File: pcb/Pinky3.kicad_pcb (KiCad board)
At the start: 2 copper layers, 137 x 100.9 mm, 65 parts, among them J1 MJ-4PP-9, P1 i2c-pin, P2 i2c-pin, SW1 RESET_SW, SW10 SW_PUSH, SW11 SW_PUSH, SW12 SW_PUSH, SW13 SW_PUSH, SW14 SW_PUSH, SW15 SW_PUSH, SW16 SW_PUSH, SW17 SW_PUSH, SW18 SW_PUSH, SW19 SW_PUSH, SW2 SW_PUSH, SW20 SW_PUSH, SW21 SW_PUSH, SW22 SW_PUSH, SW23 SW_PUSH, SW24 SW_PUSH, SW25 SW_PUSH, SW26 SW_PUSH, SW3 SW_PUSH, SW4 SW_PUSH, SW5 SW_PUSH, SW6 SW_PUSH, SW7 SW_PUSH, SW8 SW_PUSH, SW9 SW_PUSH, U1 ProMicro

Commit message: tweak
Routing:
- net Net-(J1-PadB): track 125.4 -> 126.1 mm
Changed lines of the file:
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@@
     (thickness 1.6)
     (drawings 163)
-    (tracks 955)
+    (tracks 953)
     (zones 0)
     (modules 65)
@@
     (38 B.Mask user)
     (39 F.Mask user)
-    (40 Dwgs.User user hide)
+    (40 Dwgs.User user)
     (41 Cmts.User user)
     (42 Eco1.User user)
@@
   (segment (start 164.9 107.95) (end 164.9 105.5) (width 0.25) (layer F.Cu) (net 28))
   (segment (start 102.831509 116.226489) (end 98.2 120.857998) (width 0.25) (layer F.Cu) (net 29))
-  (segment (start 98.2 133.521002) (end 96.196001 135.525001) (width 0.25) (layer F.Cu) (net 29))
-  (segment (start 98.2 120.857998) (end 98.2 133.521002) (width 0.25) (layer F.Cu) (net 29))
-  (segment (start 81.8215 134.30038) (end 81 134.30038) (width 0.25) (layer F.Cu) (net 29) (status 20))
-  (segment (start 83.046121 135.525001) (end 81.8215 134.30038) (width 0.25) (layer F.Cu) (net 29))
-  (segment (start 87.9 135.525001) (end 87.774999 135.525001) (width 0.25) (layer F.Cu) (net 29))
-  (segment (start 96.196001 135.525001) (end 87.9 135.525001) (width 0.25) (layer F.Cu) (net 29))
-  (segment (start 86.574999 135.525001) (end 86.5 135.525001) (width 0.25) (layer F.Cu) (net 29))
-  (segment (start 92.4 129.7) (end 86.574999 135.525001) (width 0.25) (layer F.Cu) (net 29) (status 10))
-  (segment (start 86.5 135.525001) (end 83.046121 135.525001) (width 0.25) (layer F.Cu) (net 29))
-  (segment (start 87.9 135.525001) (end 86.5 135.525001) (width 0.25) (layer F.Cu) (net 29))
   (segment (start 166.503122 116.196878) (end 173 109.7) (width 0.25) (layer F.Cu) (net 29))
   (segment (start 173 109.7) (end 173.4 109.7) (width 0.25) (layer F.Cu) (net 29))
@@
   (segment (start 102.831509 116.226489) (end 162.773511 116.226489) (width 0.25) (layer F.Cu) (net 29))
   (segment (start 173.4 109.7) (end 173.4 103.75) (width 0.25) (layer F.Cu) (net 29))
+  (segment (start 81.015121 134.315501) (end 81 134.315501) (width 0.25) (layer F.Cu) (net 29))
+  (segment (start 98.2 134.071002) (end 96.496001 135.775001) (width 0.25) (layer F.Cu) (net 29))
+  (segment (start 82.474621 135.775001) (end 81.015121 134.315501) (width 0.25) (layer F.Cu) (net 29))
+  (segment (start 98.2 120.857998) (end 98.2 134.071002) (width 0.25) (layer F.Cu) (net 29))
+  (segment (start 92.4 129.7) (end 86.324999 135.775001) (width 0.25) (layer F.Cu) (net 29))
+  (segment (start 86.324999 135.775001) (end 86.3 135.775001) (width 0.25) (layer F.Cu) (net 29))
+  (segment (start 86.3 135.775001) (end 82.474621 135.775001) (width 0.25) (layer F.Cu) (net 29))
+  (segment (start 96.496001 135.775001) (end 86.3 135.775001) (width 0.25) (layer F.Cu) (net 29))
   (via (at 157.9 81.9) (size 0.6) (drill 0.4) (layers F.Cu B.Cu) (net 30))
   (segment (start 52.432 118.1436) (end 49.892 118.1436) (width 0.5) (layer B.Cu) (net 30) (status 30))

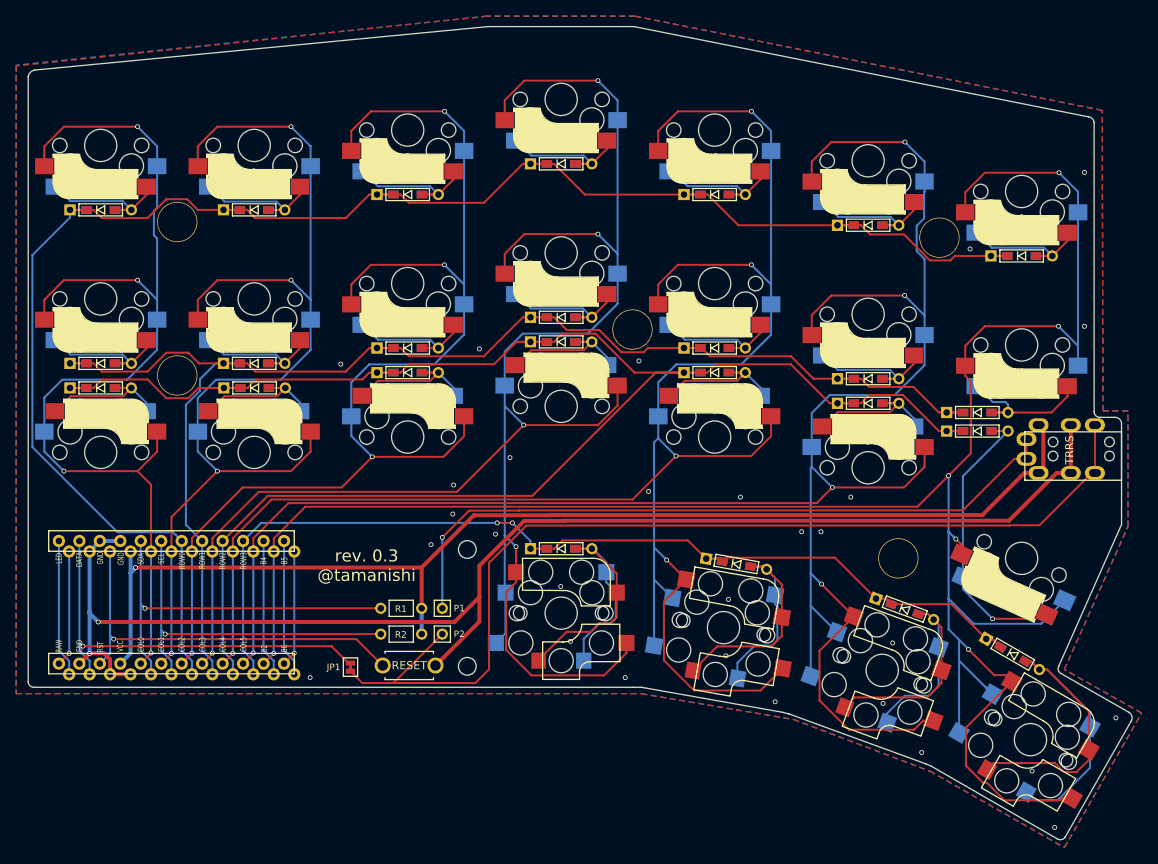
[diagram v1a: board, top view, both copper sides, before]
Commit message: - add images - add logo - change thumb keys footprints to choc only
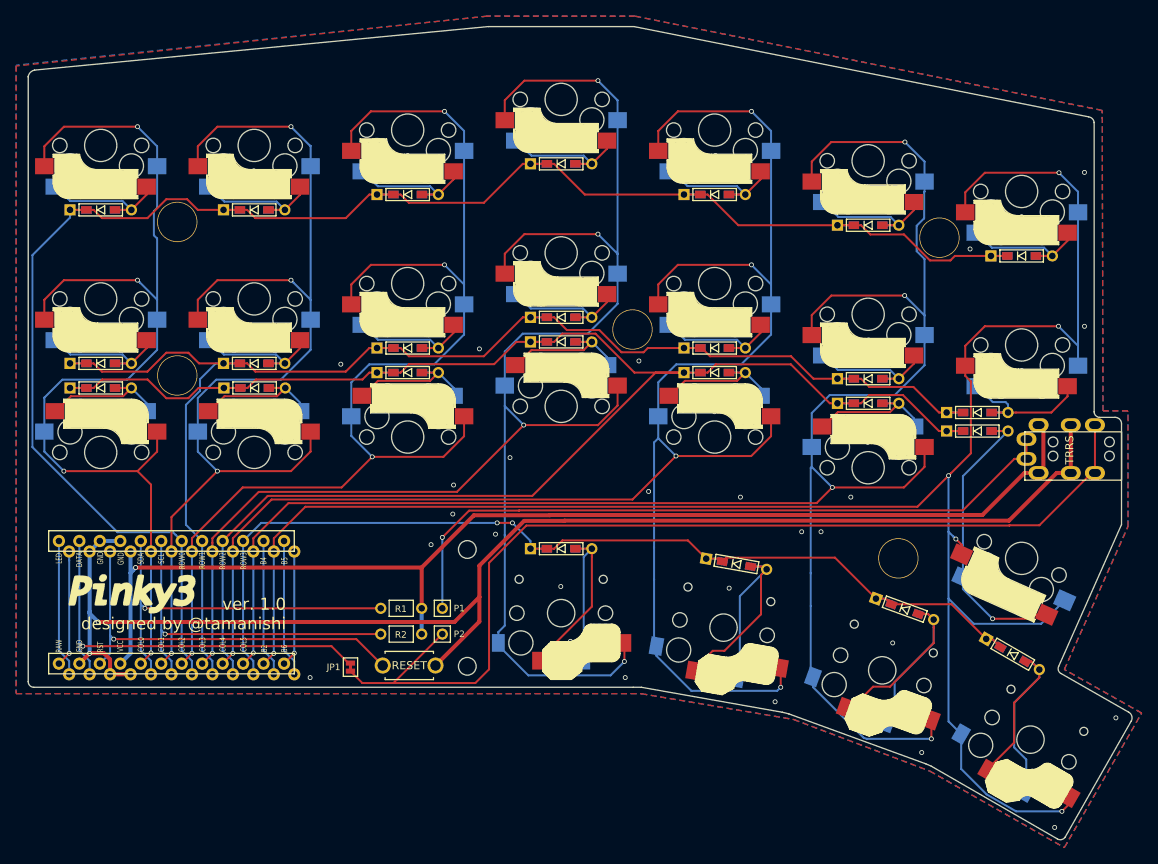
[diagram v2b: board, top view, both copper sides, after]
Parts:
- added G***: LOGO, lib:pinky3, B.Cu at (64.6, 125.7)
- added G***: LOGO, lib:pinky3, F.Cu at (53.9, 124.7)
- SW14, SW18, SW22, SW26: footprint kbd:CherryMX_KailhLowProfile_Hotswap -> kbd:Choc_Hotswap
- turned SW14 to 180 degrees
- turned SW18 to 170 degrees
- turned SW22 to 160 degrees
- turned SW26 to 150 degrees
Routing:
- net Net-(D25-Pad2): track 58.1 -> 36.6 mm
- net col6: track 272.0 -> 250.7 mm
- net col5: track 261.9 -> 242.4 mm
- net col4: track 243.4 -> 226.4 mm
- net col3: track 228.4 -> 214.8 mm
- net Net-(D13-Pad2): track 43.7 -> 35.3 mm
- net Net-(D17-Pad2): track 43.6 -> 36.5 mm, vias 1 -> 0
- net Net-(D21-Pad2): track 43.4 -> 36.8 mm
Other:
- board text added: "ver. 1.0 designed by @tamanishi"
- board text removed: "rev. 0.3 @tamanishi"

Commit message: create branch
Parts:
- D1, D10, D11, D12, D13, D14, D15, D16, D17, D18, D19, D2, D20, D21, D22, D23, D24, D25, D3, D4, D5, D6, D7, D8, D9: footprint kbd:D3_TH_SMD -> kbd:D3_SMD
- SW10, SW11, SW12, SW13, SW15, SW16, SW17, SW19, SW2, SW20, SW21, SW23, SW24, SW25, SW3, SW4, SW5, SW6, SW7, SW8, SW9: footprint kbd:CherryMX_Hotswap -> kbd:Choc_Hotswap
- moved D5 18.0 mm to (73.0, 78.5)
- moved D2 17.6 mm to (50.0, 78.5), turned to 180 degrees
- moved D4 4.25 mm to (65.0, 78.5)
- moved D3 1.55 mm to (50.0, 97.6)
- moved D1 0.55 mm to (50.0, 76.5), turned to 180 degrees
- turned SW11 to 0 degrees
- turned SW12 to 0 degrees
- turned SW15 to 0 degrees
- turned SW16 to 0 degrees
- turned SW19 to 0 degrees
- turned SW2 to 0 degrees
- turned SW20 to 0 degrees
- turned SW23 to 0 degrees
- turned SW24 to 0 degrees
- turned SW3 to 0 degrees
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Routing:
- net row0: track 213.6 -> 161.3 mm, vias 0 -> 1
- net row2: track 219.4 -> 204.1 mm
- net row1: track 178.9 -> 166.2 mm, vias 0 -> 1
- net Net-(D3-Pad2): track 18.6 -> 10.4 mm
- net Net-(D2-Pad2): track 18.4 -> 11.6 mm, vias 0 -> 2
- net Net-(D1-Pad2): track 18.7 -> 23.4 mm, vias 0 -> 2
- net col0: track 129.3 -> 133.4 mm, vias 4 -> 2

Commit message: [WIP] worked for Choc and XSwitch PCB design
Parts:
- SW14, SW18, SW22, SW26: footprint kbd:Choc_Hotswap -> lib:Kailh-PG1425-X-Switch-reversible
- moved D23 18.4 mm to (164.3, 84.6)
- moved D15 17.3 mm to (126.2, 76.9)
- moved D8 17.3 mm to (88.1, 76.9)
- moved D11 17.3 mm to (107.2, 73.1)
- moved D19 17.2 mm to (145.2, 80.8)
- moved D4 4.32 mm to (69.1, 77.0)
- moved D5 3.96 mm to (69.1, 78.8)
- moved D20 1.56 mm to (145.2, 99.5)
- moved D6 1.55 mm to (69.1, 97.6)
- moved D16 1.55 mm to (126.2, 95.7)
- moved D9 1.55 mm to (88.1, 95.7)
- moved D12 1.53 mm to (107.2, 91.9)
- moved D24 1.22 mm to (159.0, 103.3)
- moved D1 0.50 mm to (50.0, 77.0), turned to 0 degrees
- moved D2 0.30 mm to (50.0, 78.8), turned to 0 degrees
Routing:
- net row0: track 161.3 -> 196.1 mm, vias 1 -> 7
- net Net-(D21-Pad2): track 36.8 -> 15.1 mm, vias 0 -> 1
- net row1: track 166.2 -> 187.8 mm, vias 1 -> 7
- net Net-(D17-Pad2): track 36.5 -> 15.4 mm, vias 0 -> 1
- net Net-(D13-Pad2): track 35.3 -> 15.0 mm, vias 0 -> 1
- net Net-(D25-Pad2): track 36.6 -> 19.2 mm, vias 0 -> 1
- net col3: track 214.8 -> 198.5 mm
- net col5: track 242.4 -> 228.1 mm, vias 5 -> 4
- net col4: track 226.4 -> 217.1 mm, vias 5 -> 4
- net row3: track 128.8 -> 120.0 mm, vias 2 -> 6
- net Net-(D23-Pad2): track 19.6 -> 11.1 mm, vias 0 -> 2
- net Net-(D24-Pad2): track 38.2 -> 29.8 mm, vias 1 -> 2
- net Net-(D15-Pad2): track 18.4 -> 10.3 mm, vias 0 -> 2
- net Net-(D11-Pad2): track 18.4 -> 10.5 mm, vias 0 -> 2
- net Net-(D9-Pad2): track 18.6 -> 11.0 mm, vias 0 -> 2
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
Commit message: prototype pcb ordered
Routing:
- net col6: track 248.4 -> 253.8 mm
- net col5: track 228.1 -> 232.2 mm
- net row2: track 203.6 -> 200.4 mm
- net col3: track 198.5 -> 201.4 mm, vias 5 -> 4
- net col4: track 217.1 -> 214.4 mm
- net Net-(J1-PadB): track 126.1 -> 127.2 mm
- net GND: track 175.2 -> 176.0 mm
- net row3: track 120.0 -> 119.2 mm
- net VCC: track 147.1 -> 147.8 mm
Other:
- board text added: "ver. 1.0a designed by @tamanishi"
- board text removed: "ver. 1.0 designed by @tamanishi"

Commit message: tweak row2
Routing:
- net row2: track 200.4 -> 192.3 mm
- net col3: track 201.4 -> 204.8 mm, vias 4 -> 5
- net col2: track 145.2 -> 144.2 mm
- net GND: vias 56 -> 57
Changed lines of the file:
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@@
     (thickness 1.6)
     (drawings 29)
-    (tracks 910)
+    (tracks 912)
     (zones 0)
     (modules 67)
@@
   (segment (start 154.85 103.3) (end 156.325 103.3) (width 0.25) (layer F.Cu) (net 7))
   (segment (start 152.32499 100.77499) (end 154.85 103.3) (width 0.25) (layer F.Cu) (net 7))
-  (segment (start 113.876999 102.023001) (end 120.175 95.725) (width 0.25) (layer F.Cu) (net 7))
-  (segment (start 113.875001 102.023001) (end 113.876999 102.023001) (width 0.25) (layer F.Cu) (net 7))
-  (segment (start 103.073012 112.82499) (end 113.875001 102.023001) (width 0.25) (layer F.Cu) (net 7))
-  (segment (start 70.45061 112.82499) (end 103.073012 112.82499) (width 0.25) (layer F.Cu) (net 7))
-  (segment (start 65.132 118.1436) (end 70.45061 112.82499) (width 0.25) (layer F.Cu) (net 7))
   (segment (start 120.175 95.725) (end 115.643998 95.725) (width 0.25) (layer F.Cu) (net 7))
   (segment (start 120.175 95.725) (end 124.375 95.725) (width 0.25) (layer F.Cu) (net 7))
+  (segment (start 66.90061 116.37499) (end 65.893999 117.381601) (width 0.25) (layer B.Cu) (net 7))
+  (segment (start 65.893999 117.381601) (end 65.132 118.1436) (width 0.25) (layer B.Cu) (net 7))
+  (segment (start 89.550012 116.37499) (end 66.90061 116.37499) (width 0.25) (layer B.Cu) (net 7))
+  (segment (start 97.025001 108.900001) (end 89.550012 116.37499) (width 0.25) (layer B.Cu) (net 7))
+  (segment (start 97.025001 100.274999) (end 97.025001 108.900001) (width 0.25) (layer B.Cu) (net 7))
+  (segment (start 105.375 91.925) (end 97.025001 100.274999) (width 0.25) (layer B.Cu) (net 7))
   (segment (start 89.7 74.8) (end 89.875 74.8) (width 0.25) (layer B.Cu) (net 8))
   (segment (start 85.3 70.4) (end 89.7 74.8) (width 0.25) (layer B.Cu) (net 8))
@@
   (via (at 144.575 113.525) (size 0.6) (drill 0.4) (layers F.Cu B.Cu) (net 30))
   (via (at 70.475 115.125) (size 0.6) (drill 0.4) (layers F.Cu B.Cu) (net 30))
-  (via (at 65.875 114.625) (size 0.6) (drill 0.4) (layers F.Cu B.Cu) (net 30))
   (via (at 163.175 111.625) (size 0.6) (drill 0.4) (layers F.Cu B.Cu) (net 30))
+  (via (at 65.575 114.625) (size 0.6) (drill 0.4) (layers F.Cu B.Cu) (net 30))
+  (via (at 68.175 114.625) (size 0.6) (drill 0.4) (layers F.Cu B.Cu) (net 30))
   (segment (start 48.622 133.024838) (end 48.622 134.69) (width 0.25) (layer B.Cu) (net 31) (status 20))
   (segment (start 47.352 131.754838) (end 48.622 133.024838) (width 0.25) (layer B.Cu) (net 31))
@@
   (segment (start 95.85 89.2) (end 95.9 89.2) (width 0.25) (layer B.Cu) (net 38))
   (segment (start 95.9 70.4) (end 95.9 89.2) (width 0.25) (layer B.Cu) (net 38))
-  (segment (start 80.2 101.545) (end 80.2 104.198998) (width 0.25) (layer F.Cu) (net 38))
-  (segment (start 95.9 104.758002) (end 93.333002 107.325) (width 0.25) (layer B.Cu) (net 38))
-  (segment (start 95.9 101.545) (end 95.9 104.758002) (width 0.25) (layer B.Cu) (net 38))
-  (via (at 77.074499 107.324499) (size 0.6) (drill 0.4) (layers F.Cu B.Cu) (net 38))
-  (segment (start 77.075 107.325) (end 77.074499 107.324499) (width 0.25) (layer B.Cu) (net 38))
-  (segment (start 93.333002 107.325) (end 77.075 107.325) (width 0.25) (layer B.Cu) (net 38))
-  (segment (start 80.2 104.198998) (end 77.074499 107.324499) (width 0.25) (layer F.Cu) (net 38))
   (segment (start 61.322 119.45) (end 61.322 132.078) (width 0.25) (layer B.Cu) (net 38))
   (via (at 61.322 132.078) (size 0.6) (drill 0.4) (layers F.Cu B.Cu) (net 38))
   (segment (start 61.322 132.0936) (end 60.052 133.3636) (width 0.25) (layer F.Cu) (net 38))
   (segment (start 61.322 132.078) (end 61.322 132.0936) (width 0.25) (layer F.Cu) (net 38))
-  (segment (start 61.322 117.804838) (end 61.322 118.37237) (width 0.25) (layer F.Cu) (net 38))
   (segment (start 61.322 118.37237) (end 61.322 119.45) (width 0.25) (layer F.Cu) (net 38))
-  (segment (start 67.376858 111.74998) (end 61.322 117.804838) (width 0.25) (layer F.Cu) (net 38))
-  (segment (start 72.649018 111.74998) (end 67.376858 111.74998) (width 0.25) (layer F.Cu) (net 38))
-  (segment (start 77.074499 107.324499) (end 72.649018 111.74998) (width 0.25) (layer F.Cu) (net 38))
+  (segment (start 66.926848 112.19999) (end 61.322 117.804838) (width 0.25) (layer F.Cu) (net 38))
+  (segment (start 61.322 117.804838) (end 61.322 118.37237) (width 0.25) (layer F.Cu) (net 38))
+  (segment (start 74.641012 112.19999) (end 66.926848 112.19999) (width 0.25) (layer F.Cu) (net 38))
+  (segment (start 80.2 101.545) (end 80.2 106.641002) (width 0.25) (layer F.Cu) (net 38))
+  (segment (start 95.9 104.758002) (end 93.333002 107.325) (width 0.25) (layer B.Cu) (net 38))
+  (segment (start 95.9 101.545) (end 95.9 104.758002) (width 0.25) (layer B.Cu) (net 38))
+  (segment (start 79.516002 107.325) (end 79.495501 107.345501) (width 0.25) (layer B.Cu) (net 38))
+  (segment (start 93.333002 107.325) (end 79.516002 107.325) (width 0.25) (layer B.Cu) (net 38))
+  (segment (start 79.495501 107.345501) (end 74.641012 112.19999) (width 0.25) (layer F.Cu) (net 38))
+  (via (at 79.495501 107.345501) (size 0.6) (drill 0.4) (layers F.Cu B.Cu) (net 38))
+  (segment (start 80.2 106.641002) (end 79.495501 107.345501) (width 0.25) (layer F.Cu) (net 38))
   (segment (start 63.862 119.45) (end 63.862 132.072) (width 0.25) (layer B.Cu) (net 39) (status 10))
   (via (at 63.862 132.072) (size 0.6) (drill 0.4) (layers F.Cu B.Cu) (net 39))
@@
   (segment (start 110.549844 130) (end 110.550008 130.000164) (width 0.25) (layer B.Cu) (net 39))
   (segment (start 103.75 130) (end 110.549844 130) (width 0.25) (layer B.Cu) (net 39))
-  (via (at 95.675 112.19999) (size 0.6) (drill 0.4) (layers F.Cu B.Cu) (net 39))
-  (segment (start 99.25 108.62499) (end 95.675 112.19999) (width 0.25) (layer F.Cu) (net 39))
-  (segment (start 99.25 97.735) (end 99.25 108.62499) (width 0.25) (layer F.Cu) (net 39))
-  (segment (start 99.100001 115.624991) (end 95.675 112.19999) (width 0.25) (layer B.Cu) (net 39))
-  (segment (start 99.100001 125.350001) (end 99.100001 115.624991) (width 0.25) (layer B.Cu) (net 39))
   (segment (start 103.75 130) (end 99.100001 125.350001) (width 0.25) (layer B.Cu) (net 39))
-  (segment (start 63.862 117.804838) (end 63.862 118.37237) (width 0.25) (layer F.Cu) (net 39))
-  (segment (start 69.466848 112.19999) (end 63.862 117.804838) (width 0.25) (layer F.Cu) (net 39))
-  (segment (start 63.862 118.37237) (end 63.862 119.45) (width 0.25) (layer F.Cu) (net 39))
-  (segment (start 95.675 112.19999) (end 69.466848 112.19999) (width 0.25) (layer F.Cu) (net 39))
-  (segment (start 96.099264 112.19999) (end 95.675 112.19999) (width 0.25) (layer B.Cu) (net 39))
-  (segment (start 114.95 100.948002) (end 103.698012 112.19999) (width 0.25) (layer B.Cu) (net 39))
-  (segment (start 103.698012 112.19999) (end 96.099264 112.19999) (width 0.25) (layer B.Cu) (net 39))
-  (segment (start 114.95 97.735) (end 114.95 100.948002) (width 0.25) (layer B.Cu) (net 39))
+  (via (at 95.075 112.65) (size 0.6) (drill 0.4) (layers F.Cu B.Cu) (net 39))
+  (segment (start 99.25 108.475) (end 95.075 112.65) (width 0.25) (layer F.Cu) (net 39))
+  (segment (start 99.25 97.735) (end 99.25 108.475) (width 0.25) (layer F.Cu) (net 39))
+  (segment (start 99.100001 116.675001) (end 95.075 112.65) (width 0.25) (layer B.Cu) (net 39))
+  (segment (start 99.100001 125.350001) (end 99.100001 116.675001) (width 0.25) (layer B.Cu) (net 39))
+  (segment (start 107.875002 112.65) (end 95.499264 112.65) (width 0.25) (layer B.Cu) (net 39))
+  (segment (start 114.95 105.575002) (end 107.875002 112.65) (width 0.25) (layer B.Cu) (net 39))
+  (segment (start 95.499264 112.65) (end 95.075 112.65) (width 0.25) (layer B.Cu) (net 39))
+  (segment (start 114.95 97.735) (end 114.95 105.575002) (width 0.25) (layer B.Cu) (net 39))
+  (via (at 95.075 112.65) (size 0.6) (drill 0.4) (layers F.Cu B.Cu) (net 39))
+  (segment (start 63.862 117.563002) (end 63.862 119.45) (width 0.25) (layer F.Cu) (net 39))
+  (segment (start 68.775002 112.65) (end 63.862 117.563002) (width 0.25) (layer F.Cu) (net 39))
+  (segment (start 95.075 112.65) (end 68.775002 112.65) (width 0.25) (layer F.Cu) (net 39))
   (segment (start 134 63.445) (end 134 64.795) (width 0.25) (layer B.Cu) (net 40))
   (segment (start 134 82.495) (end 134 83.845) (width 0.25) (layer B.Cu) (net 40))
